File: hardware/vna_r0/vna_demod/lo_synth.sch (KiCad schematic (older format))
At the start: 1 part, among them U201 LMX2594

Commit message: work on vna r0 schematics
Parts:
- removed U201: LMX2594, symbol LMX2594
- added C? (x2): 100 nF, symbol C_Small
- added C? (x7): 1 uF, symbol C_Small
- added C? (x5): 10 uF, symbol C_Small
- added C? (x2): 10 nF, symbol C_Small
- added C? (x4): 10 pF, symbol C_Small
- added C?: 1800 pF, symbol C_Small
- added C?: DNP, symbol C_Small
- added C?: 68 nF, symbol C_Small
- added C?: 390 pF, symbol C_Small
- added L? (x2): L_Small, symbol L_Small
- added R? (x6): 22, symbol R_Small
- added R? (x4): 51, symbol R_Small
- added R?: 18, symbol R_Small
- added R?: JMP, symbol R_Small
- added R?: 68, symbol R_Small
- added U?: LMX2594, symbol LMX2594
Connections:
- net LO_A: now also C?.2
- net LO_B: now also C?.2
- net LO_C: now also C?.2
- net LO_D: now also C?.2
- net SYNTH_REF: now also C?.1
- new net: R?.1, U?.1 (CE)
- new net: C?.2, U?.10 (VregIN)
- new net: R?.1, U?.16 (SCK)
- new net: R?.1, U?.17 (SDI)
- new net: R?.1, U?.20 (MUXout)
- new net: R?.2, U?.24 (CSB)
- new net: C?.1, U?.27 (VbiasVCO2)
- new net: C?.1, U?.29 (VrefVCO2)
- new net: C?.1, U?.3 (VbiasVCO)
- new net: C?.1, U?.33 (VbiasVARAC)
- new net: C?.1, R?.1, U?.35 (Vtune)
- new net: C?.1, U?.36 (VrefVCO)
- new net: C?.1, U?.38 (VreVCO)
- new net: R?.1, U?.5 (SYNC)
- new net: C?.2, U?.8 (OSCinP)
- new net: C?.2, L?.2, R?.1, R?.2 (x2)
- new net: C?.1, R?.1, R?.2
- new net: C?.2, R?.1
- new net +3V3: C?.1, C?.2, C?.2, C?.2, C?.2, C?.2, L?.1, L?.1, U?.11 (VccCP), U?.15 (VccMASH), U?.21 (VccBUF), U?.26 (VccVCO2), U?.37 (VccVCO), U?.7 (VccDIG)
- new net CPOUT: C?.1, C?.1, R?.2, U?.12 (CPout)
- new net GND: C?.1, C?.1, C?.1, C?.1, C?.1, C?.1, C?.1, C?.1, C?.2, C?.2, C?.2, C?.2, C?.2, C?.2, C?.2, C?.2, C?.2, C?.2, R?.2, R?.2, U?.13 (GND), U?.14 (GND), U?.2 (GND), U?.25 (GND), U?.28 (SysRefReq), U?.30 (RampClk), U?.31 (GND), U?.32 (RampDir), U?.34 (GND), U?.39 (GND), U?.4 (GND), U?.40 (GND), U?.41 (GND), U?.6 (GND)
- new net LMX_CE: R?.2
- new net LMX_CSB: R?.1
- new net LMX_MUXout: R?.2
- new net LMX_SCK: R?.2
- new net LMX_SDI: R?.2
- new net RFOUTAM: C?.1, R?.1, U?.22 (RFoutAM)
- new net RFOUTAP: C?.1, R?.2, U?.23 (RFoutAP)
- new net RFOUTBM: C?.1, R?.1, U?.18 (RFoutBM)
- new net RFOUTBP: C?.1, R?.2, U?.19 (RFoutBP)
- no-connect marks 0 -> 1

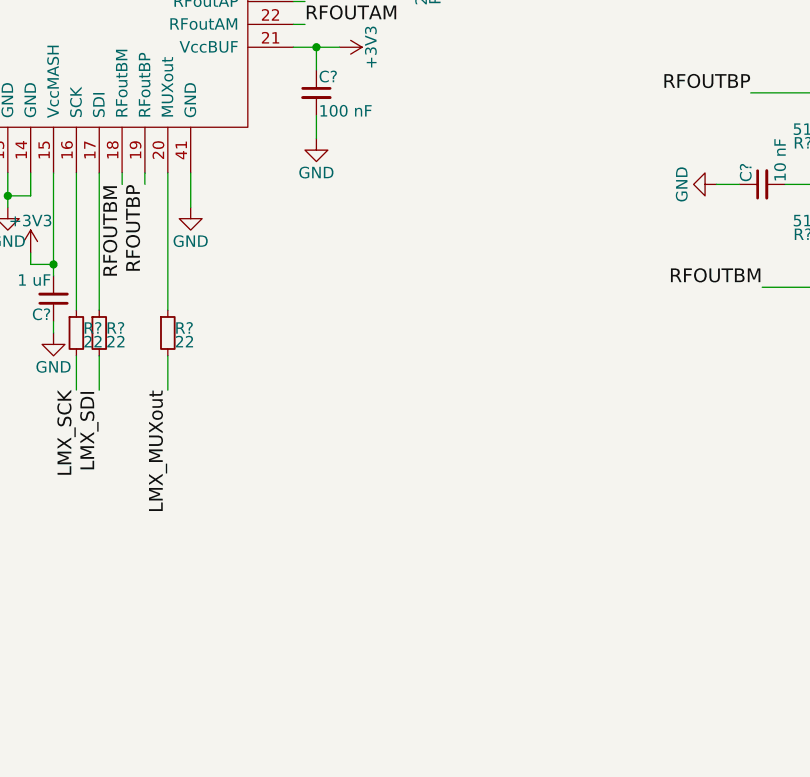
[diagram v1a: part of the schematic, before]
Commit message: finished vna r0 demod schematic
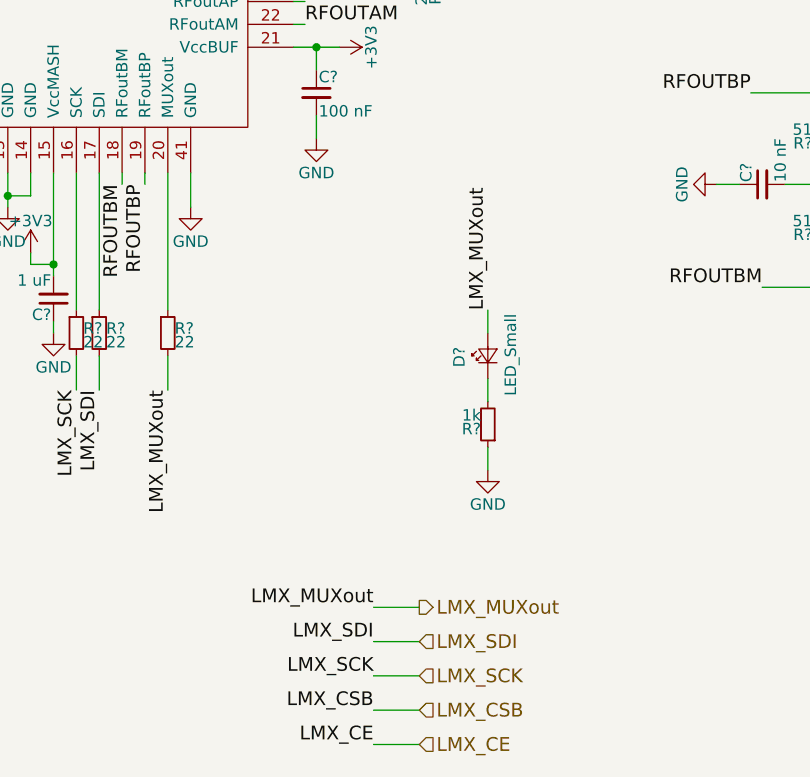
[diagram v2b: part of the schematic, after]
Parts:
- added D?: LED_Small, symbol LED_Small
- added R?: 1k, symbol R_Small
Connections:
- net GND: now also R?.1
- net LMX_MUXout: now also D?.2 (A)
- new net: D?.1 (K), R?.2
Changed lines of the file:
@@
 Wire Wire Line
 	3950 5350 3950 5150
+$Comp
+L LED_Small D?
+U 1 1 593F76AB
+P 6150 5950
+F 0 "D?" H 6100 6075 50  0000 L CNN
+F 1 "LED_Small" H 5975 5850 50  0000 L CNN
+F 2 "" V 6150 5950 50  0001 C CNN
+F 3 "" V 6150 5950 50  0001 C CNN
+	1    6150 5950
+	0    -1   -1   0
+$EndComp
+$Comp
+L R_Small R?
+U 1 1 593F7872
+P 6150 6250
+F 0 "R?" H 6180 6270 50  0000 L CNN
+F 1 "1k" H 6180 6210 50  0000 L CNN
+F 2 "" H 6150 6250 50  0001 C CNN
+F 3 "" H 6150 6250 50  0001 C CNN
+	1    6150 6250
+	-1   0    0    1
+$EndComp
+$Comp
+L GND #PWR?
+U 1 1 593F7956
+P 6150 6450
+F 0 "#PWR?" H 6150 6200 50  0001 C CNN
+F 1 "GND" H 6150 6300 50  0000 C CNN
+F 2 "" H 6150 6450 50  0001 C CNN
+F 3 "" H 6150 6450 50  0001 C CNN
+	1    6150 6450
+	1    0    0    -1
+$EndComp
+Wire Wire Line
+	6150 6350 6150 6450
+Wire Wire Line
+	6150 6150 6150 6050
+Wire Wire Line
+	6150 5750 6150 5850
+Text HLabel 5850 7050 2    60   Output ~ 0
+LMX_MUXout
+Text HLabel 5850 7200 2    60   Input ~ 0
+LMX_SDI
+Text HLabel 5850 7350 2    60   Input ~ 0
+LMX_SCK
+Text HLabel 5850 7500 2    60   Input ~ 0
+LMX_CSB
+Text HLabel 5850 7650 2    60   Input ~ 0
+LMX_CE
+Text Label 5650 7500 2    60   ~ 0
+LMX_CSB
+Text Label 5650 7650 2    60   ~ 0
+LMX_CE
+Text Label 5650 7200 2    60   ~ 0
+LMX_SDI
+Text Label 5650 7050 2    60   ~ 0
+LMX_MUXout
+Text Label 6150 5750 1    60   ~ 0
+LMX_MUXout
+Text Label 5650 7350 2    60   ~ 0
+LMX_SCK
+Wire Wire Line
+	5650 7650 5850 7650
+Wire Wire Line
+	5650 7500 5850 7500
+Wire Wire Line
+	5650 7350 5850 7350
+Wire Wire Line
+	5650 7200 5850 7200
+Wire Wire Line
+	5650 7050 5850 7050
 $EndSCHEMATC

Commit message: footprint assignment on vna r0
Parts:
- C201, C202, C204, C205, C206, C207, C209, C210, C211, C213, C214, C215, C218, C219, C220, C221, C222, C223, C224: renamed from C?; footprint (none) -> Capacitors_SMD:C_0402
- C203, C208, C212, C216, C217: renamed from C?; footprint (none) -> Capacitors_SMD:C_0603
- D201: renamed from D?; footprint (none) -> LEDs:LED_0603
- L201, L202: renamed from L?; footprint (none) -> Resistors_SMD:R_0402
- R201, R202, R203, R204, R205, R206, R207, R208, R209, R210, R211, R212, R213, R214: renamed from R?; footprint (none) -> Resistors_SMD:R_0402
- U201: renamed from U?; footprint (none) -> Housings_DFN_QFN:QFN-40-1EP_6x6mm_Pitch0.5mm

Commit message: started on routing demod for vna r0
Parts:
- added J201: RF_Shield_Two_Pieces, Shielding_Cabinets:Laird_Technologies_BMI-S-209-F_29.36x18.50mm, symbol RF_Shield_Two_Pieces
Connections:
- net GND: now also J201.1 (Shield)
- net LO_A: now also C222.2; no longer C223.2
- net LO_B: now also C221.2; no longer C224.2
- net LO_C: now also C224.2; no longer C221.2
- net LO_D: now also C223.2; no longer C222.2
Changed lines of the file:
@@
 Comment4 ""
 $EndDescr
+Text HLabel 9050 5650 2    60   Output ~ 0
+LO_A
+Text HLabel 9000 4800 2    60   Output ~ 0
+LO_B
+Text HLabel 9050 3850 2    60   Output ~ 0
+LO_C
 Text HLabel 9050 3000 2    60   Output ~ 0
-LO_A
-Text HLabel 9050 3850 2    60   Output ~ 0
-LO_B
-Text HLabel 9000 4800 2    60   Output ~ 0
-LO_C
-Text HLabel 9050 5650 2    60   Output ~ 0
 LO_D
 $Comp
@@
 Wire Wire Line
 	5650 7050 5850 7050
+$Comp
+L RF_Shield_Two_Pieces J201
+U 1 1 594EE123
+P 9500 1250
+F 0 "J201" H 9500 1450 50  0000 C CNN
+F 1 "RF_Shield_Two_Pieces" H 9500 1350 50  0000 C CNN
+F 2 "Shielding_Cabinets:Laird_Technologies_BMI-S-209-F_29.36x18.50mm" H 9500 1150 50  0001 C CNN
+F 3 "" H 9500 1150 50  0001 C CNN
+	1    9500 1250
+	1    0    0    -1
+$EndComp
+$Comp
+L GND #PWR041
+U 1 1 594EE3AD
+P 9500 1750
+F 0 "#PWR041" H 9500 1500 50  0001 C CNN
+F 1 "GND" H 9500 1600 50  0000 C CNN
+F 2 "" H 9500 1750 50  0001 C CNN
+F 3 "" H 9500 1750 50  0001 C CNN
+	1    9500 1750
+	1    0    0    -1
+$EndComp
+Wire Wire Line
+	9500 1750 9500 1650
 $EndSCHEMATC

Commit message: removed unnecessary dc blocking caps on demod synth
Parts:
- removed C221, C222, C223, C224: 10 pF, Capacitors_SMD:C_0402, symbol C_Small
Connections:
- net RFOUTAM is gone; now on net LO_C: R214.1, U201.22 (RFoutAM)
- net RFOUTAP is gone; now on net LO_D: R213.2, U201.23 (RFoutAP)
- net RFOUTBM is gone; now on net LO_A: R212.1, U201.18 (RFoutBM)
- net RFOUTBP is gone; now on net LO_B: R211.2, U201.19 (RFoutBP)
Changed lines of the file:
@@
-$EndComp
-$Comp
-L C_Small C223
-U 1 1 593E6B9B
-P 8000 3000
-F 0 "C223" H 8010 3070 50  0000 L CNN
-F 1 "10 pF" H 8010 2920 50  0000 L CNN
-F 2 "Capacitors_SMD:C_0402" H 8000 3000 50  0001 C CNN
-F 3 "" H 8000 3000 50  0001 C CNN
-	1    8000 3000
-	0    -1   -1   0
-$EndComp
-$Comp
-L C_Small C224
-U 1 1 593E6BA5
-P 8000 3850
-F 0 "C224" H 8010 3920 50  0000 L CNN
-F 1 "10 pF" H 8010 3770 50  0000 L CNN
-F 2 "Capacitors_SMD:C_0402" H 8000 3850 50  0001 C CNN
-F 3 "" H 8000 3850 50  0001 C CNN
-	1    8000 3850
-	0    -1   -1   0
 $EndComp
 $Comp
@@
 $EndComp
 $Comp
-L C_Small C221
-U 1 1 593E6BCE
-P 7950 4800
-F 0 "C221" H 7960 4870 50  0000 L CNN
-F 1 "10 pF" H 7960 4720 50  0000 L CNN
-F 2 "Capacitors_SMD:C_0402" H 7950 4800 50  0001 C CNN
-F 3 "" H 7950 4800 50  0001 C CNN
-	1    7950 4800
-	0    -1   -1   0
-$EndComp
-$Comp
-L C_Small C222
-U 1 1 593E6BD8
-P 7950 5650
-F 0 "C222" H 7960 5720 50  0000 L CNN
-F 1 "10 pF" H 7960 5570 50  0000 L CNN
-F 2 "Capacitors_SMD:C_0402" H 7950 5650 50  0001 C CNN
-F 3 "" H 7950 5650 50  0001 C CNN
-	1    7950 5650
-	0    -1   -1   0
-$EndComp
-$Comp
 L GND #PWR036
 U 1 1 593E6BE2
@@
 	3200 4000 3300 4000
 Wire Wire Line
-	8100 3000 9050 3000
-Wire Wire Line
-	8100 3850 9050 3850
-Wire Wire Line
-	8050 4800 9000 4800
-Wire Wire Line
-	8050 5650 9050 5650
+	7500 3000 9050 3000
+Wire Wire Line
+	7400 3850 9050 3850
+Wire Wire Line
+	7300 4800 9000 4800
+Wire Wire Line
+	7350 5650 9050 5650
 Wire Wire Line
 	5300 4600 5500 4600
@@
 	7200 3400 7300 3400
 Wire Wire Line
-	7900 3000 7500 3000
-Wire Wire Line
 	7650 3000 7650 3100
 Connection ~ 7650 3000
 Wire Wire Line
-	7900 3850 7400 3850
-Wire Wire Line
 	7650 3700 7650 3850
 Connection ~ 7650 3850
@@
 	7950 5200 8050 5200
 Wire Wire Line
-	7300 4800 7850 4800
-Wire Wire Line
 	7600 4800 7600 4900
 Connection ~ 7600 4800
 Wire Wire Line
-	7850 5650 7350 5650
-Wire Wire Line
 	7600 5500 7600 5650

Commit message: vna r0 schematic cleanup
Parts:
- D201: value LED_Small -> RED
- J201: value RF_Shield_Two_Pieces -> BMI-S-209
- L201, L202: value L_Small -> 22 nH
- R201, R202, R205, R206, R207, R209: value 22 -> 1k
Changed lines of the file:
@@
 U 1 1 593E6A2D
 P 4350 5850
-F 0 "R205" H 4380 5870 50  0000 L CNN
-F 1 "22" H 4380 5810 50  0000 L CNN
+F 0 "R205" V 4400 6000 50  0000 L CNN
+F 1 "1k" V 4400 5650 50  0000 L CNN
 F 2 "Resistors_SMD:R_0402" H 4350 5850 50  0001 C CNN
 F 3 "" H 4350 5850 50  0001 C CNN
@@
 U 1 1 593E6A36
 P 4450 5850
-F 0 "R206" H 4480 5870 50  0000 L CNN
-F 1 "22" H 4480 5810 50  0000 L CNN
+F 0 "R206" V 4550 5550 50  0000 L CNN
+F 1 "1k" V 4550 5800 50  0000 L CNN
 F 2 "Resistors_SMD:R_0402" H 4450 5850 50  0001 C CNN
 F 3 "" H 4450 5850 50  0001 C CNN
@@
 P 4750 5850
 F 0 "R207" H 4780 5870 50  0000 L CNN
-F 1 "22" H 4780 5810 50  0000 L CNN
+F 1 "1k" H 4780 5810 50  0000 L CNN
 F 2 "Resistors_SMD:R_0402" H 4750 5850 50  0001 C CNN
 F 3 "" H 4750 5850 50  0001 C CNN
@@
 P 5900 4300
 F 0 "R209" H 5930 4320 50  0000 L CNN
-F 1 "22" H 5930 4260 50  0000 L CNN
+F 1 "1k" H 5930 4260 50  0000 L CNN
 F 2 "Resistors_SMD:R_0402" H 5900 4300 50  0001 C CNN
 F 3 "" H 5900 4300 50  0001 C CNN
@@
 U 1 1 593E6A55
 P 2850 3700
-F 0 "R201" H 2880 3720 50  0000 L CNN
-F 1 "22" H 2880 3660 50  0000 L CNN
+F 0 "R201" V 2750 3700 50  0000 L CNN
+F 1 "1k" V 2750 3550 50  0000 L CNN
 F 2 "Resistors_SMD:R_0402" H 2850 3700 50  0001 C CNN
 F 3 "" H 2850 3700 50  0001 C CNN
@@
 U 1 1 593E6B35
 P 2850 4100
-F 0 "R202" H 2880 4120 50  0000 L CNN
-F 1 "22" H 2880 4060 50  0000 L CNN
+F 0 "R202" V 2950 4000 50  0000 L CNN
+F 1 "1k" V 2950 3850 50  0000 L CNN
 F 2 "Resistors_SMD:R_0402" H 2850 4100 50  0001 C CNN
 F 3 "" H 2850 4100 50  0001 C CNN
@@
 U 1 1 593E6B45
 P 2850 3900
-F 0 "C203" H 2860 3970 50  0000 L CNN
-F 1 "10 uF" H 2860 3820 50  0000 L CNN
+F 0 "C203" V 2800 3650 50  0000 L CNN
+F 1 "10 uF" V 2900 3650 50  0000 L CNN
 F 2 "Capacitors_SMD:C_0603" H 2850 3900 50  0001 C CNN
 F 3 "" H 2850 3900 50  0001 C CNN
@@
 P 7350 5200
 F 0 "C219" H 7360 5270 50  0000 L CNN
-F 1 "10 nF" H 7360 5120 50  0000 L CNN
+F 1 "10 nF" V 7200 5150 50  0000 L CNN
 F 2 "Capacitors_SMD:C_0402" H 7350 5200 50  0001 C CNN
 F 3 "" H 7350 5200 50  0001 C CNN
@@
 P 7900 3400
 F 0 "L202" H 7930 3440 50  0000 L CNN
-F 1 "L_Small" H 7930 3360 50  0000 L CNN
+F 1 "22 nH" H 7930 3360 50  0000 L CNN
 F 2 "Resistors_SMD:R_0402" H 7900 3400 50  0001 C CNN
 F 3 "" H 7900 3400 50  0001 C CNN
@@
 U 1 1 593E6B7C
 P 7650 3200
-F 0 "R213" H 7680 3220 50  0000 L CNN
-F 1 "51" H 7680 3160 50  0000 L CNN
+F 0 "R213" H 7400 3200 50  0000 L CNN
+F 1 "51" H 7500 3100 50  0000 L CNN
 F 2 "Resistors_SMD:R_0402" H 7650 3200 50  0001 C CNN
 F 3 "" H 7650 3200 50  0001 C CNN
@@
 P 7850 5200
 F 0 "L201" H 7880 5240 50  0000 L CNN
-F 1 "L_Small" H 7880 5160 50  0000 L CNN
+F 1 "22 nH" H 7880 5160 50  0000 L CNN
 F 2 "Resistors_SMD:R_0402" H 7850 5200 50  0001 C CNN
 F 3 "" H 7850 5200 50  0001 C CNN
@@
 P 6150 5950
 F 0 "D201" H 6100 6075 50  0000 L CNN
-F 1 "LED_Small" H 5975 5850 50  0000 L CNN
+F 1 "RED" H 5975 5850 50  0000 L CNN
 F 2 "LEDs:LED_0603" V 6150 5950 50  0001 C CNN
 F 3 "" V 6150 5950 50  0001 C CNN
@@
 P 9500 1250
 F 0 "J201" H 9500 1450 50  0000 C CNN
-F 1 "RF_Shield_Two_Pieces" H 9500 1350 50  0000 C CNN
+F 1 "BMI-S-209" H 9500 1350 50  0000 C CNN
 F 2 "Shielding_Cabinets:Laird_Technologies_BMI-S-209-F_29.36x18.50mm" H 9500 1150 50  0001 C CNN
 F 3 "" H 9500 1150 50  0001 C CNN
